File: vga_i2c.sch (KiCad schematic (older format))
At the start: 22 parts, among them J1 VGA DB15 Female, J2 VGA DB15 Male, J3 Atari 2600 Joystick DB9, J4 Conn_01x06, J5 Jumpers, J6 Conn_01x13, SW1 SW_Push, SW2 SW_Push, SW3 SW_Push, U1 MCP23017_SP

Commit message: Version 1
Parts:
- removed J2: VGA DB15 Male, symbol Connector:DB15_Male_HighDensity_MountingHoles
- added C1, C2: C, Capacitors_SMD:C_0603_HandSoldering, symbol Device:C
- added J7: VGA DB15 Female, 181-015-213R561:NORCOMP_181-015-213R561, symbol Connector:DB15_Female_HighDensity_MountingHoles
- added R10, R11, R12, R13, R14: 10K, Resistors_SMD:R_0603_HandSoldering, symbol Device:R
- added SW4: SW Up, Buttons_Switches_ThroughHole:SW_PUSH_6mm, symbol Switch:SW_Push
- added SW5: SW Down, Buttons_Switches_ThroughHole:SW_PUSH_6mm, symbol Switch:SW_Push
- added SW6: SW Left, Buttons_Switches_ThroughHole:SW_PUSH_6mm, symbol Switch:SW_Push
- added SW7: SW Right, Buttons_Switches_ThroughHole:SW_PUSH_6mm, symbol Switch:SW_Push
- added SW8: SW Trigger, Buttons_Switches_ThroughHole:SW_PUSH_6mm, symbol Switch:SW_Push
- D1, D2, D3: footprint (none) -> LEDs:LED_0805_HandSoldering
- J1: footprint (none) -> 181-015-213R561:NORCOMP_181-015-213R561
- J3: footprint (none) -> 1-1634580-2:TE_1-1634580-2
- J4: footprint (none) -> Pin_Headers:Pin_Header_Straight_1x06_Pitch2.54mm
- J5: footprint (none) -> Pin_Headers:Pin_Header_Straight_2x04_Pitch2.54mm
- J6: footprint (none) -> Pin_Headers:Pin_Header_Straight_1x13_Pitch2.54mm
- R1, R2, R3, R4, R5, R6, R7, R8, R9: footprint (none) -> Resistors_SMD:R_0603_HandSoldering
- SW1, SW2, SW3: footprint (none) -> Buttons_Switches_ThroughHole:SW_PUSH_6mm
- U1: footprint Package_DIP:DIP-28_W7.62mm -> Housings_DIP:DIP-28_W7.62mm_LongPads
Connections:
- wire segments 134 -> 203
- no-connect marks 4 -> 6

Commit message: !st production version.
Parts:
- removed SW4: SW Up, Buttons_Switches_ThroughHole:SW_PUSH_6mm, symbol Switch:SW_Push
- removed SW5: SW Down, Buttons_Switches_ThroughHole:SW_PUSH_6mm, symbol Switch:SW_Push
- removed SW6: SW Left, Buttons_Switches_ThroughHole:SW_PUSH_6mm, symbol Switch:SW_Push
- removed SW7: SW Right, Buttons_Switches_ThroughHole:SW_PUSH_6mm, symbol Switch:SW_Push
- removed SW8: SW Trigger, Buttons_Switches_ThroughHole:SW_PUSH_6mm, symbol Switch:SW_Push
- removed U1: MCP23017_SP, Housings_DIP:DIP-28_W7.62mm_LongPads, symbol Interface_Expansion:MCP23017_SP
- added U1: MCP23017_SO, Housings_SOIC:SOIC-28W_7.5x18.7mm_Pitch1.27mm, symbol Interface_Expansion:MCP23017_SO
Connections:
- net labels added: rstn
- wire segments 203 -> 193
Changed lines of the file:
@@
-$EndComp
-$Comp
-L Interface_Expansion:MCP23017_SP U1
-U 1 1 5C39C310
-P 5450 4800
-F 0 "U1" H 5750 5900 50  0000 C CNN
-F 1 "MCP23017_SP" H 5800 5800 50  0000 C CNN
-F 2 "Housings_DIP:DIP-28_W7.62mm_LongPads" H 5650 3800 50  0001 L CNN
-F 3 "http://ww1.microchip.com/downloads/en/DeviceDoc/20001952C.pdf" H 5650 3700 50  0001 L CNN
-	1    5450 4800
-	1    0    0    -1
 $EndComp
 $Comp
@@
 paddle_b
 Wire Wire Line
+	6700 5300 6150 5300
+Wire Wire Line
+	6700 5200 6150 5200
+Wire Wire Line
+	6700 5100 6150 5100
+Wire Wire Line
+	6700 5000 6150 5000
+Wire Wire Line
 	6700 4900 6150 4900
-Wire Wire Line
-	6700 5300 6150 5300
-Wire Wire Line
-	6700 5000 6150 5000
-Wire Wire Line
-	6700 5100 6150 5100
-Wire Wire Line
-	6700 5200 6150 5200
+Text Label 6250 5300 0    50   ~ 0
+up
+Text Label 6250 5200 0    50   ~ 0
+trigger
+Text Label 6250 5100 0    50   ~ 0
+down
+Text Label 6250 5000 0    50   ~ 0
+left
 Text Label 6250 4900 0    50   ~ 0
-up
-Text Label 6250 5300 0    50   ~ 0
-trigger
-Text Label 6250 5000 0    50   ~ 0
-down
-Text Label 6250 5100 0    50   ~ 0
-left
-Text Label 6250 5200 0    50   ~ 0
 right
 Wire Wire Line
@@
 Wire Wire Line
 	1250 3200 1700 3200
-$Comp
-L Switch:SW_Push SW4
-U 1 1 5C459C59
-P 8900 2700
-F 0 "SW4" H 8750 2800 50  0000 C CNN
-F 1 "SW Up" H 9100 2800 50  0000 C CNN
-F 2 "Buttons_Switches_ThroughHole:SW_PUSH_6mm" H 8900 2900 50  0001 C CNN
-F 3 "" H 8900 2900 50  0001 C CNN
-	1    8900 2700
-	1    0    0    -1
-$EndComp
-$Comp
-L Switch:SW_Push SW5
-U 1 1 5C465829
-P 8900 2900
-F 0 "SW5" H 8750 3000 50  0000 C CNN
-F 1 "SW Down" H 9100 3000 50  0000 C CNN
-F 2 "Buttons_Switches_ThroughHole:SW_PUSH_6mm" H 8900 3100 50  0001 C CNN
-F 3 "" H 8900 3100 50  0001 C CNN
-	1    8900 2900
-	1    0    0    -1
-$EndComp
-$Comp
-L Switch:SW_Push SW6
-U 1 1 5C471405
-P 8900 3100
-F 0 "SW6" H 8750 3200 50  0000 C CNN
-F 1 "SW Left" H 9100 3200 50  0000 C CNN
-F 2 "Buttons_Switches_ThroughHole:SW_PUSH_6mm" H 8900 3300 50  0001 C CNN
-F 3 "" H 8900 3300 50  0001 C CNN
-	1    8900 3100
-	1    0    0    -1
-$EndComp
-$Comp
-L Switch:SW_Push SW7
-U 1 1 5C47CFD5
-P 8900 3300
-F 0 "SW7" H 8750 3400 50  0000 C CNN
-F 1 "SW Right" H 9100 3400 50  0000 C CNN
-F 2 "Buttons_Switches_ThroughHole:SW_PUSH_6mm" H 8900 3500 50  0001 C CNN
-F 3 "" H 8900 3500 50  0001 C CNN
-	1    8900 3300
-	1    0    0    -1
-$EndComp
-$Comp
-L Switch:SW_Push SW8
-U 1 1 5C488C50
-P 8900 3500
-F 0 "SW8" H 8750 3600 50  0000 C CNN
-F 1 "SW Trigger" H 9100 3600 50  0000 C CNN
-F 2 "Buttons_Switches_ThroughHole:SW_PUSH_6mm" H 8900 3700 50  0001 C CNN
-F 3 "" H 8900 3700 50  0001 C CNN
-	1    8900 3500
-	1    0    0    -1
-$EndComp
-Wire Wire Line
-	8700 2700 8150 2700
-Wire Wire Line
-	8700 3500 8150 3500
-Wire Wire Line
-	8700 2900 8150 2900
-Wire Wire Line
-	8700 3100 8150 3100
-Wire Wire Line
-	8700 3300 8150 3300
 Text Label 8250 2700 0    50   ~ 0
 up
-Text Label 8250 3500 0    50   ~ 0
-trigger
 Text Label 8250 2900 0    50   ~ 0
 down
@@
 Text Label 8250 3300 0    50   ~ 0
 right
-$Comp
-L power:GND #PWR03
-U 1 1 5C4EA82C
-P 9300 3700
-F 0 "#PWR03" H 9300 3450 50  0001 C CNN
-F 1 "GND" H 9305 3527 50  0000 C CNN
-F 2 "" H 9300 3700 50  0001 C CNN
-F 3 "" H 9300 3700 50  0001 C CNN
-	1    9300 3700
-	1    0    0    -1
-$EndComp
-Wire Wire Line
-	9100 3500 9300 3500
-Wire Wire Line
-	9300 3500 9300 3700
-Wire Wire Line
-	9100 3300 9300 3300
-Wire Wire Line
-	9300 3300 9300 3500
-Connection ~ 9300 3500
-Wire Wire Line
-	9100 3100 9300 3100
-Wire Wire Line
-	9300 3100 9300 3300
-Connection ~ 9300 3300
-Wire Wire Line
-	9100 2900 9300 2900
-Wire Wire Line
-	9300 2900 9300 3100
-Connection ~ 9300 3100
-Wire Wire Line
-	9100 2700 9300 2700
-Wire Wire Line
-	9300 2700 9300 2900
-Connection ~ 9300 2900
 $Comp
 L Device:R R10
@@
 Wire Wire Line
 	6950 5000 6950 5400
+$Comp
+L Interface_Expansion:MCP23017_SO U1
+U 1 1 5C37B2E0
+P 5450 4800
+F 0 "U1" H 5450 6078 50  0000 C CNN
+F 1 "MCP23017_SO" H 5450 5987 50  0000 C CNN
+F 2 "Housings_SOIC:SOIC-28W_7.5x18.7mm_Pitch1.27mm" H 5650 3800 50  0001 L CNN
+F 3 "http://ww1.microchip.com/downloads/en/DeviceDoc/20001952C.pdf" H 5650 3700 50  0001 L CNN
+	1    5450 4800
+	1    0    0    -1
+$EndComp
+Text Label 8250 3500 0    50   ~ 0
+trigger
+Wire Wire Line
+	8700 3300 8150 3300
+Wire Wire Line
+	8700 3100 8150 3100
+Wire Wire Line
+	8700 2900 8150 2900
+Wire Wire Line
+	8700 3500 8150 3500
+Wire Wire Line
+	8700 2700 8150 2700
+Text Label 4600 4900 0    50   ~ 0
+rstn
 $EndSCHEMATC

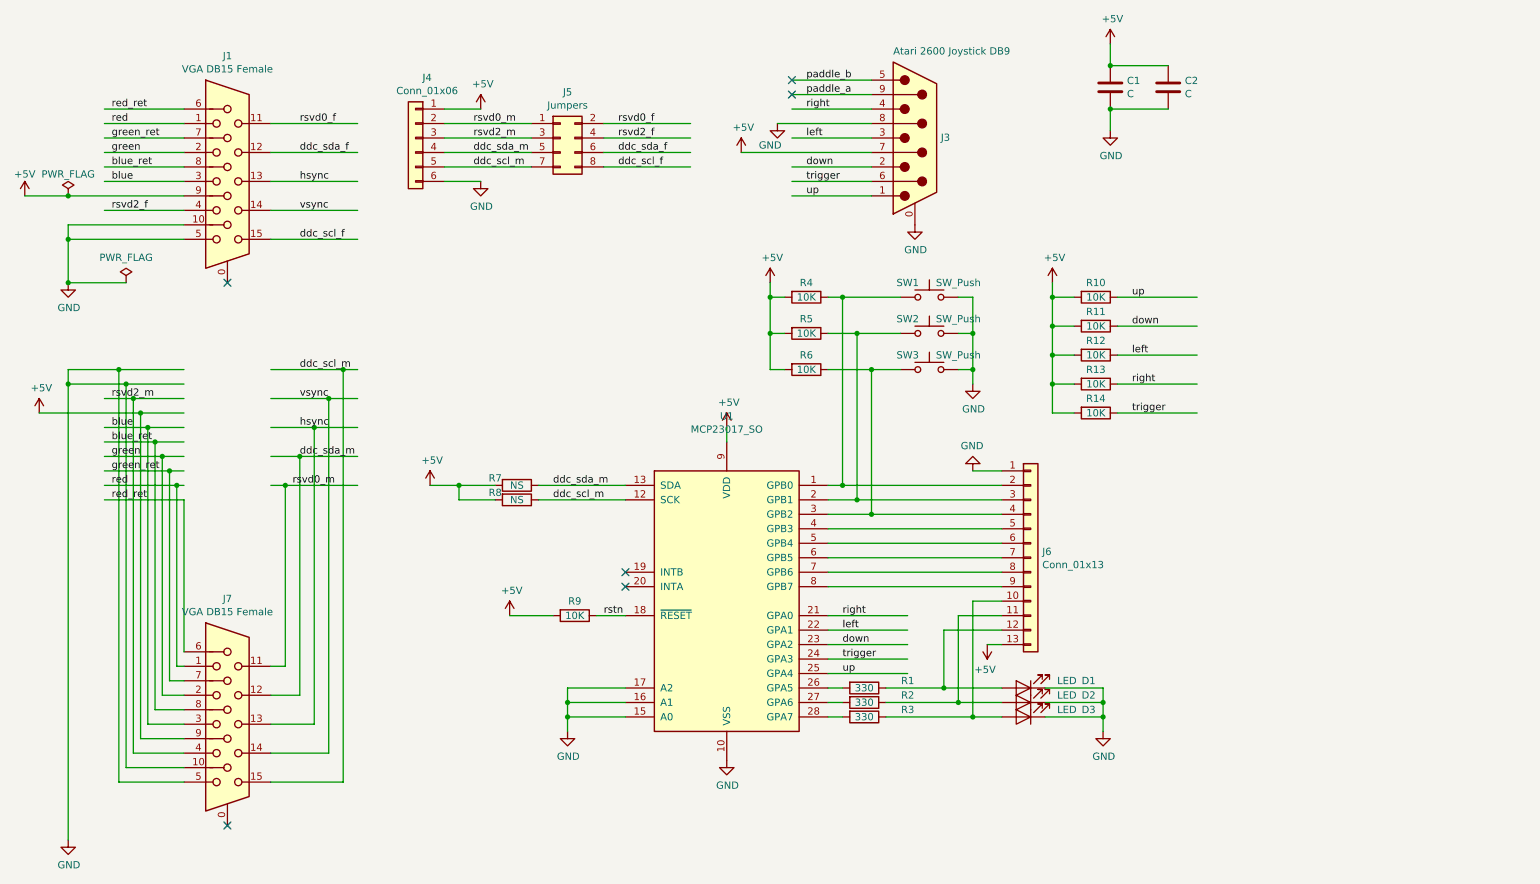
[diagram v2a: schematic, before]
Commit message: Version with 2 joysticks.
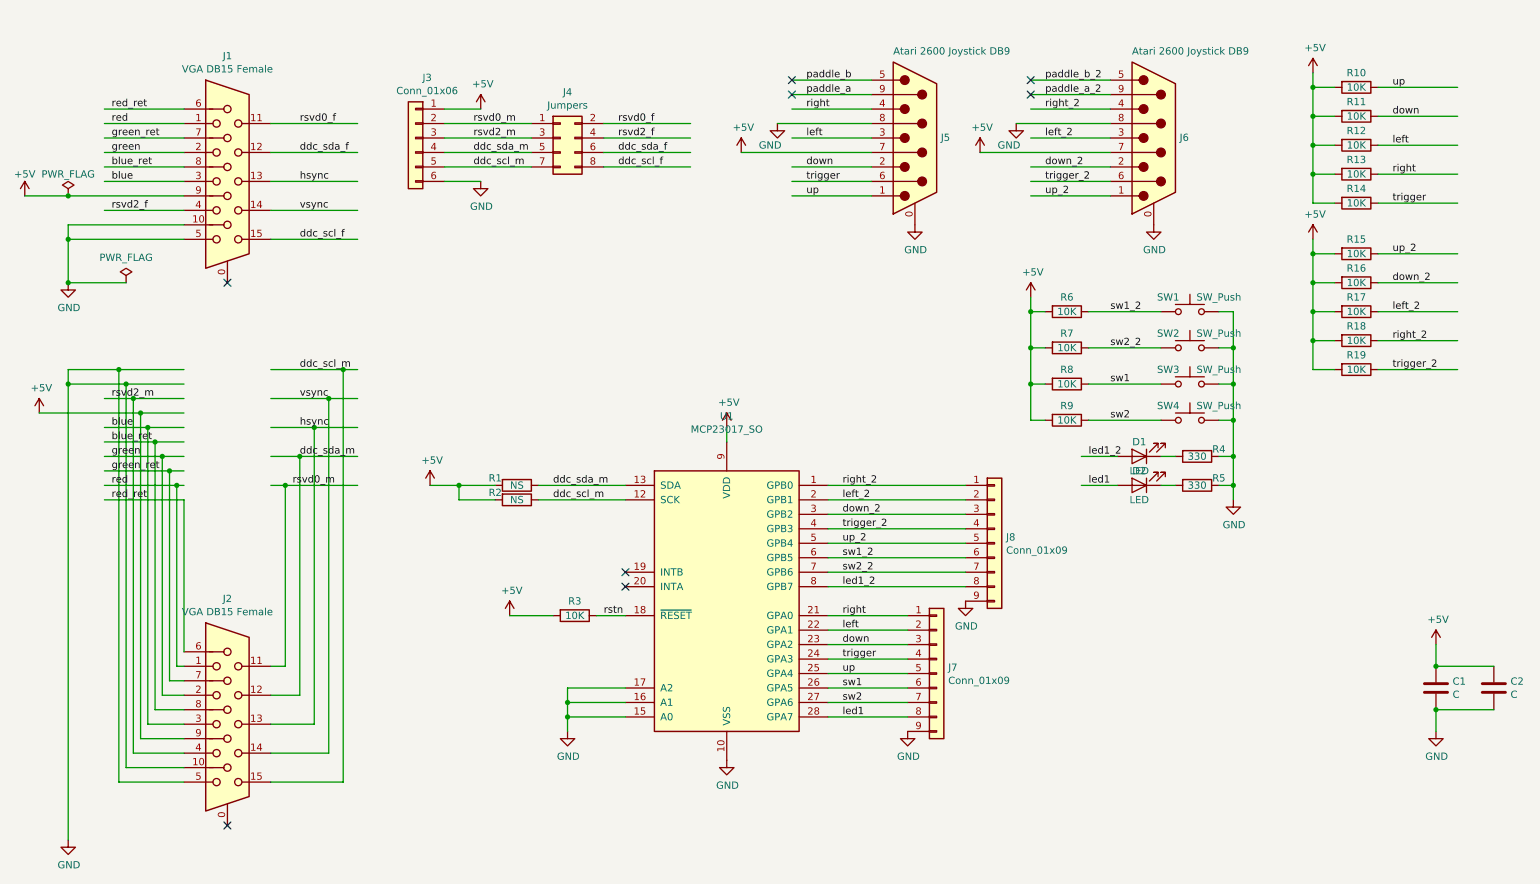
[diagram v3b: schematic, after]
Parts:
- removed D2: LED, LEDs:LED_0805_HandSoldering, symbol Device:LED
- removed J6: Conn_01x13, Pin_Headers:Pin_Header_Straight_1x13_Pitch2.54mm, symbol Connector_Generic:Conn_01x13
- removed R1, R2: 330, Resistors_SMD:R_0603_HandSoldering, symbol Device:R
- removed SW3: SW_Push, Buttons_Switches_ThroughHole:SW_PUSH_6mm, symbol Switch:SW_Push
- added J6: Atari 2600 Joystick DB9, 1-1634580-2:TE_1-1634580-2, symbol Connector:DB9_Male_MountingHoles
- added J7, J8: Conn_01x09, Pin_Headers:Pin_Header_Straight_1x09_Pitch2.54mm, symbol Connector_Generic:Conn_01x09
- added R15, R16, R17, R18, R19, R7: 10K, Resistors_SMD:R_0603_HandSoldering, symbol Device:R
- added R4: 330, Resistors_SMD:R_0603_HandSoldering, symbol Device:R
- added SW1, SW2: SW_Push, Buttons_Switches_ThroughHole:SW_PUSH_6mm, symbol Switch:SW_Push
- renumbered D3 to D2, J7 to J2, J4 to J3, J5 to J4, J3 to J5, R7 to R1, R8 to R2, R9 to R3, R3 to R5, R4 to R8, R5 to R9, SW1 to SW3, SW2 to SW4
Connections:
- net labels added: down_2, led1, led1_2, left_2, paddle_a_2, paddle_b_2, right_2, sw1, sw1_2, sw2, sw2_2, trigger_2, up_2
- wire segments 193 -> 201
- no-connect marks 6 -> 8
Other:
- moved on the sheet: C1, C2, D2, R10, R11, R12, R13, R14, R5, R8, R9, SW3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
